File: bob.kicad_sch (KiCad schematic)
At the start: 55 parts, among them J1 Micro USB Female, J2 Screw Terminal, 2.54mm, J3 GPIO (Optional), J4 GPIO (Optional), J5 Conn_01x03_Male, J6 Conn_01x06_Pin, Q1 AO3400A, SW1 Bootsel, U1 AMS1117-3.3, U2 W25Q128JVSS, U3 QMC5883L, U4 HP203B, U5 RP2040, U6 QMI8658C, U7 W25Q128JVSS, Y1 12MHz

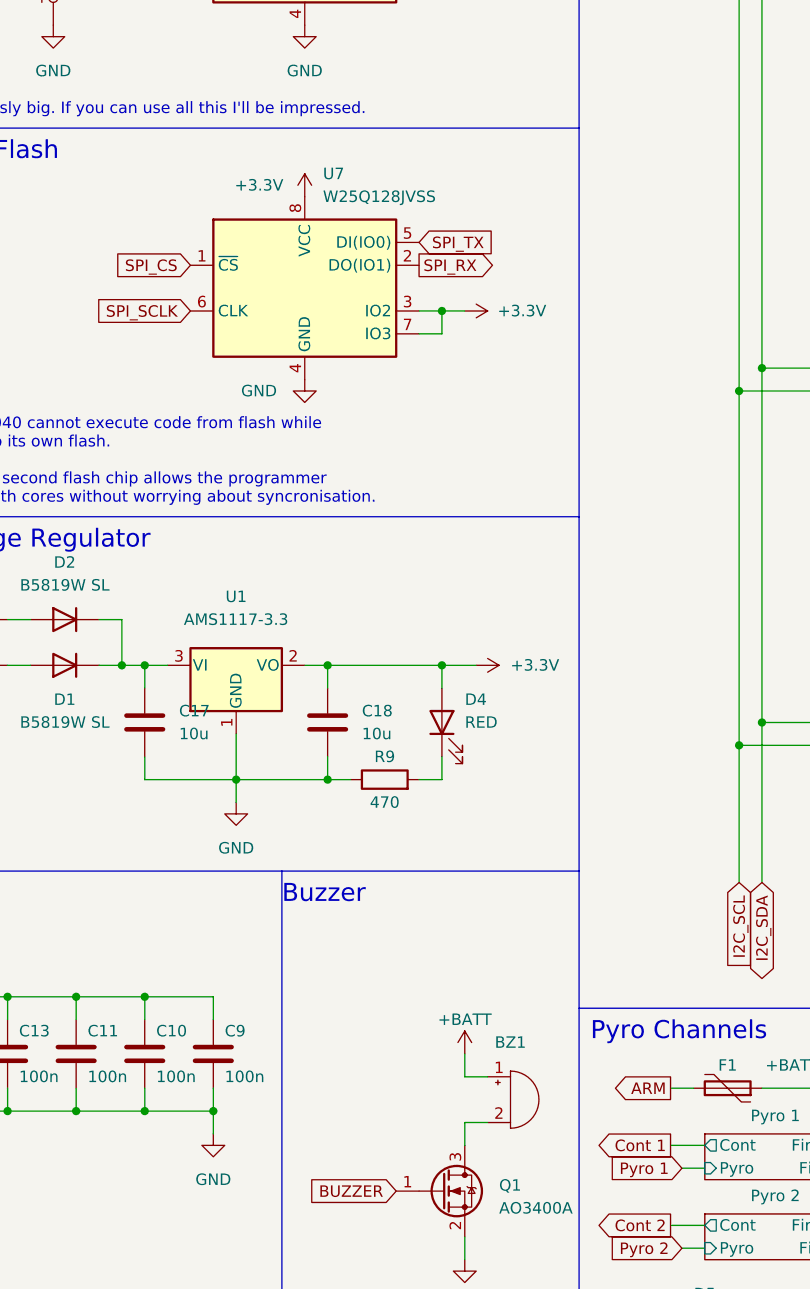
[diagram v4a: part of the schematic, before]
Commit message: Change to piezo buzzer in stock, add parallel resistor per manufacturer's guidance
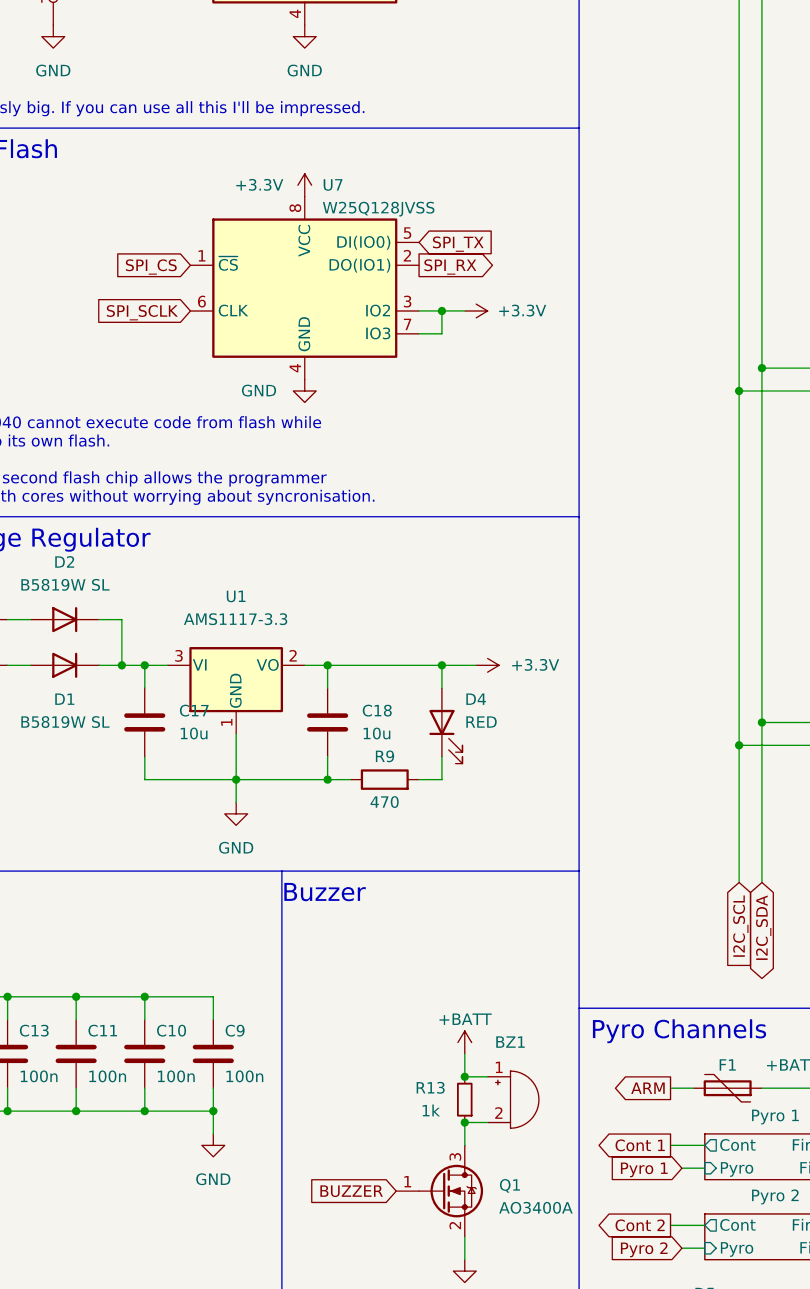
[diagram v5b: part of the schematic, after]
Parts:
- added R13: 1k, Resistor_SMD:R_0603_1608Metric, symbol Device:R_Small
- BZ1: footprint YAR_other:Cy-SMD-4020-3040 -> YAR_other:CPT-7502-65-SMT-TR
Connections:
- net +BATT: now also R13.2
- net at BZ1.2 (+), Q1.3 (D): now also R13.1
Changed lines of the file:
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@@
   (junction (at 109.22 162.56) (diameter 0) (color 0 0 0 0)
   )
+  (junction (at 182.88 163.83) (diameter 0) (color 0 0 0 0)
+  )
+  (junction (at 182.88 158.75) (diameter 0) (color 0 0 0 0)
+  )
   (junction (at 180.34 73.66) (diameter 0) (color 0 0 0 0)
   )
@@
     (stroke (width 0) (type default))
   )
-  (wire (pts (xy 182.88 163.83) (xy 185.42 163.83))
-    (stroke (width 0) (type default))
-  )
   (wire (pts (xy 81.28 21.59) (xy 81.28 24.13))
     (stroke (width 0) (type default))
@@
     (stroke (width 0) (type default))
   )
+  (wire (pts (xy 182.88 156.21) (xy 182.88 158.75))
+    (stroke (width 0) (type default))
+  )
   (wire (pts (xy 154.94 165.1) (xy 154.94 162.56))
     (stroke (width 0) (type default))
@@
     (stroke (width 0) (type default))
   )
+  (wire (pts (xy 185.42 163.83) (xy 182.88 163.83))
+    (stroke (width 0) (type default))
+  )
   (wire (pts (xy 180.34 76.2) (xy 180.34 73.66))
     (stroke (width 0) (type default))
@@
     (stroke (width 0) (type default))
   )
-  (wire (pts (xy 182.88 156.21) (xy 182.88 158.75))
-    (stroke (width 0) (type default))
-  )
   (wire (pts (xy 74.93 21.59) (xy 77.47 21.59))
     (stroke (width 0) (type default))
@@
     (stroke (width 0) (type default))
   )
-  (wire (pts (xy 182.88 158.75) (xy 185.42 158.75))
-    (stroke (width 0) (type default))
-  )
   (wire (pts (xy 101.6 182.88) (xy 101.6 185.42))
     (stroke (width 0) (type default))
@@
     (stroke (width 0) (type default))
   )
+  (wire (pts (xy 182.88 158.75) (xy 185.42 158.75))
+    (stroke (width 0) (type default))
+  )
   (wire (pts (xy 132.08 149.86) (xy 132.08 152.4))
     (stroke (width 0) (type default))
@@
       (effects (font (size 1.27 1.27)) (justify right) hide)
     )
-    (property "Footprint" "YAR_other:Cy-SMD-4020-3040" (at 187.325 158.75 90)
+    (property "Footprint" "YAR_other:CPT-7502-65-SMT-TR" (at 187.325 158.75 90)
       (effects (font (size 1.27 1.27)) hide)
     )
@@
     )
   )
+  (symbol (lib_id "Device:R_Small") (at 182.88 161.29 180) (unit 1)
+    (in_bom yes) (on_board yes) (dnp no)
+    (property "Reference" "R13" (at 179.07 160.02 0)
+      (effects (font (size 1.27 1.27)))
+    )
+    (property "Value" "1k" (at 179.07 162.56 0)
+      (effects (font (size 1.27 1.27)))
+    )
+    (property "Footprint" "Resistor_SMD:R_0603_1608Metric" (at 182.88 161.29 0)
+      (effects (font (size 1.27 1.27)) hide)
+    )
+    (property "Datasheet" "~" (at 182.88 161.29 0)
+      (effects (font (size 1.27 1.27)) hide)
+    )
+    (property "JLC" "0603" (at 182.88 161.29 0)
+      (effects (font (size 1.27 1.27)) hide)
+    )
+    (property "LCSC" "C21190" (at 182.88 161.29 0)
+      (effects (font (size 1.27 1.27)) hide)
+    )
+    (pin "1")
+    (pin "2")
+    (instances
+      (project "bob"
+        (path "/febb7d9c-f8af-428a-b455-1415daa5c3f8"
+          (reference "R13") (unit 1)
+        )
+      )
+    )
+  )
   (symbol (lib_id "power:GND") (at 113.03 127 0) (unit 1)
     (in_bom yes) (on_board yes) (dnp no) (fields_autoplaced)
@@
   (symbol (lib_id "Memory_Flash:W25Q32JVSS") (at 165.1 71.12 0) (unit 1)
     (in_bom yes) (on_board yes) (dnp no) (fields_autoplaced)
-    (property "Reference" "U7" (at 167.1194 58.42 0)
+    (property "Reference" "U7" (at 167.0559 59.69 0)
       (effects (font (size 1.27 1.27)) (justify left))
     )
-    (property "Value" "W25Q128JVSS" (at 167.1194 60.96 0)
+    (property "Value" "W25Q128JVSS" (at 167.0559 62.23 0)
       (effects (font (size 1.27 1.27)) (justify left))
     )
